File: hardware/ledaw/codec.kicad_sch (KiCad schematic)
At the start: 50 parts, among them U1 MAX98089ETN_T, Y1 SG-210SCD

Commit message: hw: headphone and wip mic
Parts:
- removed TP1: JACKSENSE, symbol Connector:TestPoint_2Pole
- removed TP11: FSPKRN, symbol Connector:TestPoint_2Pole
- removed TP2: RXP, symbol Connector:TestPoint_2Pole
- removed TP3: RXN, symbol Connector:TestPoint_2Pole
- removed TP5: FSPKLP, symbol Connector:TestPoint_2Pole
- removed TP7: FSPKLN, symbol Connector:TestPoint_2Pole
- removed TP9: FSPKRP, symbol Connector:TestPoint_2Pole
- added C16, C17: 10pF, symbol Device:C_Small
- added C18: 2.2uF, symbol Device:C_Small
- added C19, C20, C21, C22: 1uF, symbol Device:C_Small
- added J1: HEADPHONE, symbol Connector_Audio:AudioJack3_Ground
- added JP1, JP2, JP3: (no value), symbol Jumper:Jumper_2_Small_Open
- added R11, R12, R13, R14: 0, symbol Device:R_Small
- added R15: OPEN, symbol Device:R_Small
- added R16: 10k, symbol Device:R_Small
- added R17, R18: 2.2k, symbol Device:R_Small
- added TP1: JACKSENSE, symbol Connector:TestPoint
- added TP11: FSPKRN, symbol Connector:TestPoint
- added TP12: HPR, symbol Connector:TestPoint
- added TP13: HPL, symbol Connector:TestPoint
- added TP14: HPGND, symbol Connector:TestPoint
- added TP2: RXP, symbol Connector:TestPoint
- added TP3: RXN, symbol Connector:TestPoint
- added TP5: FSPKLP, symbol Connector:TestPoint
- added TP7: FSPKLN, symbol Connector:TestPoint
- added TP9: FSPKRP, symbol Connector:TestPoint
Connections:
- net GND: now also R5.2, U1.16 (SPKRGND), U1.21 (SPKLGND), U1.3 (DGND), U1.30 (HPGND), U1.47 (AGND), U1.57 (EP), C16.2, C17.2, C18.2, C19.2, C21.1, C22.1
- net JACKSNS: now also JP3.1 (A), TP1.1
- net at C5.1, C7.2, L2.2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: now also TP7.1
- net at C15.1, C9.1, L3.2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: now also TP9.1
- net at C1.1, L1.1, TP4.1: now also R7.1; no longer R3.1
- net at C2.1, C7.1, L1.2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: now also TP5.1
- net at R2.1: now also TP3.1
- net at C8.1, L3.1, TP8.1: now also R11.1; no longer R7.1
- net at R7.2: now also U1.20 (SPKLP); no longer U1.17 (SPKRP)
- net at C4.1, L2.1, TP6.1: now also R9.1; no longer R5.1
- net at C11.1, L4.1, TP10.1: now also R12.1; no longer R9.1
- net at C13.1, C15.2, L4.2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: now also TP11.1
- net at R9.2: now also U1.22 (SPKLN); no longer U1.15 (SPKRN)
- net HPGND: now reaches R3.2
- net HPGND: now also R5.1, J1.G, TP14.1; no longer U1.20 (SPKLP)
- net C1P: now reaches U1.26 (C1P)
- net C1P: now also C20.2
- net C1N: now reaches U1.27 (C1N)
- net C1N: now also C20.1
- net HPVSS: now reaches U1.31 (HPVSS)
- net HPVSS: now also C21.2
- net HPVDD: now reaches U1.32 (HPVDD)
- net at U1.33 (HPL): now also C17.1, R14.2
- net at U1.34 (HPSNS): now also R3.1
- net at U1.35 (HPR): now also C16.1, R13.2
- net at U1.44 (MICBIAS): now also C22.2, JP2.2 (B), R18.1
- net at U1.48 (REF): now also C18.1
- net at U1.49 (REG): now also C19.1
- net CODEC_~{IRQ}: now reaches U1.56 (~{IRQ})
- net CODEC_~{IRQ}: now also R15.1, R16.1
- net at R1.1: now also TP2.1
- new net: J1.R, R13.1, TP12.1
- new net: J1.S, JP1.2 (B)
- new net: R12.2, U1.15 (SPKRN)
- new net: JP3.2 (B), R17.2
- new net: J1.T, R14.1, TP13.1
- new net: JP2.1 (A), R17.1
- new net: R11.2, U1.17 (SPKRP)
- new net +1V8: R15.2
- new net +3V3: R16.2
- new net MIC1P: JP1.1 (A)
- new net MIC2P: R18.2
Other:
- note added: "TODO conn HPND pin to net?"
- moved on the sheet: TP4

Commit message: hw: big simplification
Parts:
- removed C100: 10uF, symbol Device:C_Small
- removed C16, C17: 10pF, symbol Device:C_Small
- removed C22: 1uF, symbol Device:C_Small
- removed J1: HEADPHONE, symbol Connector_Audio:AudioJack3_Ground
- removed JP1, JP2, JP3: (no value), symbol Jumper:Jumper_2_Small_Open
- removed R13, R14, R3, R5: 0, symbol Device:R_Small
- removed R15: OPEN, symbol Device:R_Small
- removed R18: 2.2k, symbol Device:R_Small
- added C108, C109: 1uF, symbol Device:C_Small
- added C23: 10uF, symbol Device:C_Small
- added J2: AudioJack4, symbol Connector_Audio:AudioJack4
- added TP15: MIC2P, symbol Connector:TestPoint
- added TP16: MIC2N, symbol Connector:TestPoint
- added TP17: MICBIAS, symbol Connector:TestPoint
- added TP18: HPSNS, symbol Connector:TestPoint
- C102, C106: value 1uF -> 0.1uF
- C12: value 0.1uF -> 1uF
- TP2: value RXP -> RECP
- TP3: value RXN -> RECN
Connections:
- net AVDD is gone; now on net +1V8: C103.2, U1.50 (AVDD)
- net DVDD is gone; now on net +1V8: C101.2, U1.53 (DVDD)
- net DVDDS1 is gone; now on net +3V3: C102.2, U1.6 (DVDDS1)
- net DVDDS2 is gone; now on net +3V3: C106.2, U1.55 (DVDDS2)
- net JACKSNS is gone; now on net JackS: TP1.1, U1.45 (JACKSNS)
- net PVDD is gone; now on net +1V8: C12.2, U1.25 (PVDD)
- net +1V8: now also C23.2
- net GND: now also U1.34 (HPSNS), C109.1, C23.1, J2.R2, TP16.1, TP18.1
- net at TP12.1: now also U1.35 (HPR), J2.R1
- net at U1.33 (HPL): now also TP13.1, J2.T
- net at U1.44 (MICBIAS): now also R17.1
- net JackS: now reaches R17.2
- net JackS: now also C108.1, J2.S, TP15.1, TP17.1
- net at U1.42 (MIC2P): now also C108.2
- net at U1.43 (MIC2N): now also C109.2
- net SPKVDD renamed +5V
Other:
- moved on the sheet: C107, R16, TP12, TP13, Y1

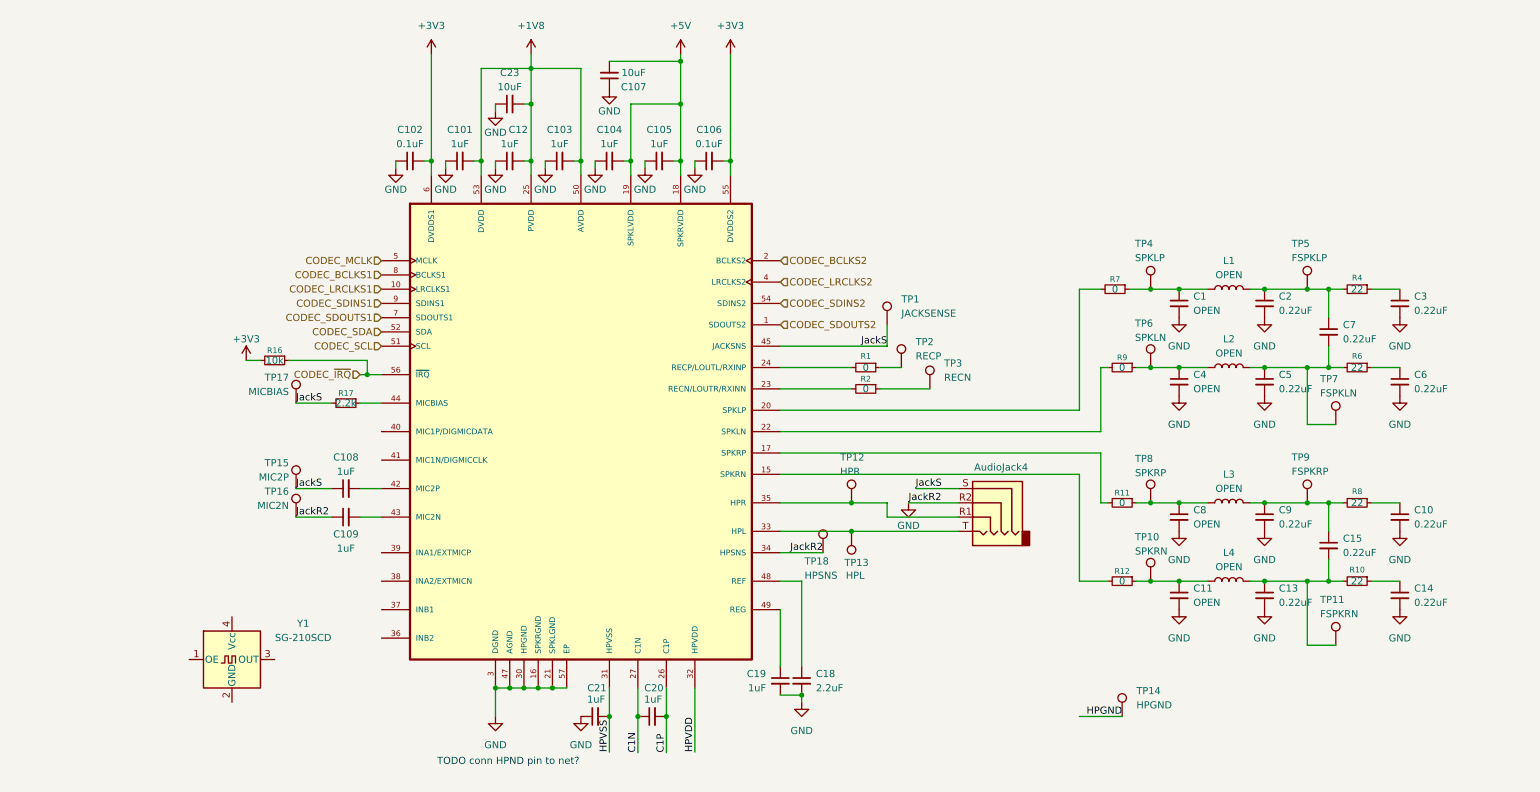
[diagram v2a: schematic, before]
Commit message: hw: speakers, line in/out. only missing digital mic now
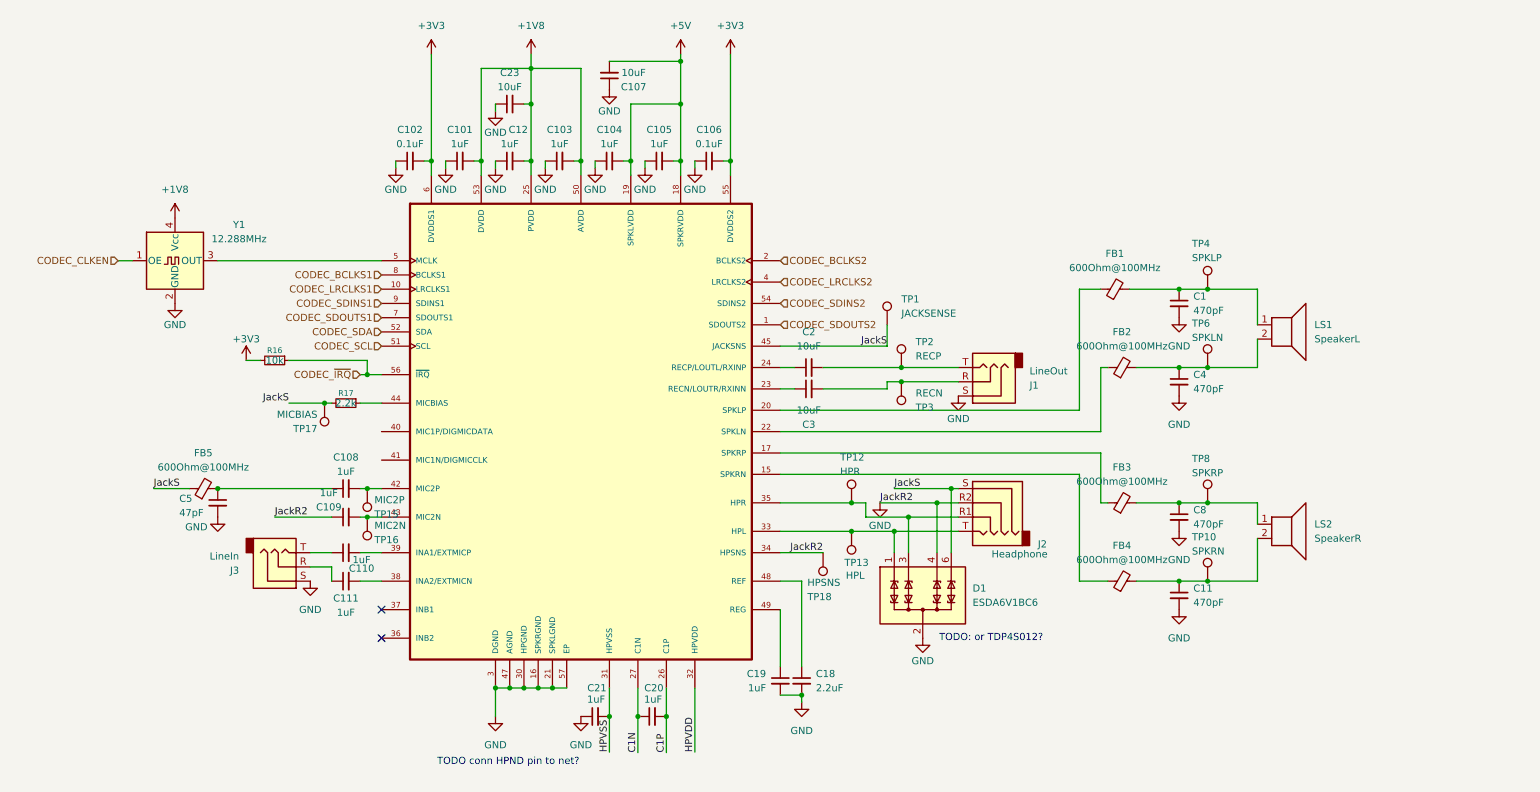
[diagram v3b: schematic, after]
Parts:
- removed C10, C13, C14, C15, C6, C7, C9: 0.22uF, symbol Device:C_Small
- removed L1, L2, L3, L4: OPEN, symbol Device:L
- removed R1, R11, R12, R2, R7, R9: 0, symbol Device:R_Small
- removed R10, R4, R6, R8: 22, symbol Device:R_Small
- removed TP11: FSPKRN, symbol Connector:TestPoint
- removed TP14: HPGND, symbol Connector:TestPoint
- removed TP5: FSPKLP, symbol Connector:TestPoint
- removed TP7: FSPKLN, symbol Connector:TestPoint
- removed TP9: FSPKRP, symbol Connector:TestPoint
- added C110, C111: 1uF, symbol Device:C_Small
- added D1: ESDA6V1BC6, Package_TO_SOT_SMD:SOT-23-6, symbol Power_Protection:ESDA6V1BC6
- added FB1, FB2, FB3, FB4, FB5: 600Ohm@100MHz, symbol Device:FerriteBead_Small
- added J1: LineOut, symbol Connector_Audio:AudioJack3
- added J3: LineIn, symbol Connector_Audio:AudioJack3
- added LS1: SpeakerL, symbol Device:Speaker
- added LS2: SpeakerR, symbol Device:Speaker
- C1, C11, C4, C8: value OPEN -> 470pF
- C2, C3: value 0.22uF -> 10uF
- C5: value 0.22uF -> 47pF
- J2: value AudioJack4 -> Headphone
- Y1: value SG-210SCD -> 12.288MHz
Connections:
- net CODEC_MCLK is gone; now on an unnamed net: U1.5 (MCLK)
- net +1V8: now also Y1.4 (Vcc)
- net GND: now also Y1.2 (GND), D1.2 (COM), D1.4 (TVS3), D1.5 (COM), J1.S, J3.S; no longer C2.2, C3.2, TP16.1
- net JackS: now also D1.6 (TVS4), FB5.1; no longer C108.1, TP15.1
- net at J2.R1, TP12.1, U1.35 (HPR): now also D1.3 (TVS2)
- net at C5.1: now also C108.1, FB5.2
- net at J2.T, TP13.1, U1.33 (HPL): now also D1.1 (TVS1)
- net at C1.1, TP4.1: now also FB1.2, LS1.1
- net at C2.1: now also U1.24 (RECP/LOUTL/RXINP)
- net at C4.1, TP6.1: now also FB2.2, LS1.2
- net at U1.22 (SPKLN): now also FB2.1
- net at TP3.1: now also C3.2, J1.R
- net at U1.23 (RECN/LOUTR/RXINN): now also C3.1
- net at C8.1, TP8.1: now also FB3.2, LS2.1
- net at C11.1, TP10.1: now also FB4.2, LS2.2
- net at U1.15 (SPKRN): now also FB4.1
- net at TP2.1: now also C2.2, J1.T
- net at U1.20 (SPKLP): now also FB1.1
- net CODEC_CLKEN: now reaches Y1.1 (OE)
- net at U1.17 (SPKRP): now also FB3.1
- net at U1.38 (INA2/EXTMICN): now also C111.2
- net at U1.39 (INA1/EXTMICP): now also C110.2
- net at C108.2, U1.42 (MIC2P): now also TP15.1
- net at C109.2, U1.43 (MIC2N): now also TP16.1
- new net: C110.1, J3.T
- new net: C111.1, J3.R
- no-connect marks 0 -> 2
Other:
- note added: "TODO: or TDP4S012?"
- moved on the sheet: TP10, TP18, TP4, TP6, TP8, Y1

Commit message: hw: done codec?
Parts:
- added C22: 1uF, symbol Device:C_Small
- added C6, C7: 0.1uF X7R, symbol Device:C_Small
- added MK1: MicL, Sensor_Audio:Knowles_LGA-5_3.5x2.65mm, symbol Sensor_Audio:SPH0641LU4H-1
- added MK2: MicR, Sensor_Audio:Knowles_LGA-5_3.5x2.65mm, symbol Sensor_Audio:SPH0641LU4H-1
- added TP19: CODEC_MCLK, symbol Connector:TestPoint
- added TP20: INA1, symbol Connector:TestPoint
- added TP21: INA2, symbol Connector:TestPoint
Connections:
- net CODEC_SDINS2 is gone; now on net GND: U1.54 (SDINS2)
- net +1V8: now also C6.2, C7.2, MK1.5 (VDD), MK2.2 (SEL), MK2.5 (VDD)
- net GND: now also C21.2, C22.2, C6.1, C7.1, MK1.2 (SEL), MK1.3 (GND), MK2.3 (GND); no longer C21.1
- net at C110.2, U1.39 (INA1/EXTMICP): now also TP20.1
- net at U1.5 (MCLK), Y1.3 (OUT): now also TP19.1
- net at C111.2, U1.38 (INA2/EXTMICN): now also TP21.1
- net DIGMICDATA: now reaches U1.40 (MIC1P/DIGMICDATA)
- net DIGMICDATA: now also MK1.1 (DATA), MK2.1 (DATA)
- net DIGMICCLK: now reaches U1.41 (MIC1N/DIGMICCLK)
- net DIGMICCLK: now also MK1.4 (CLOCK), MK2.4 (CLOCK)
- net CODEC_BCLKS2: no longer names the net of U1.2 (BCLKS2)
- net CODEC_LRCLKS2: no longer names the net of U1.4 (LRCLKS2)
- net CODEC_SDOUTS2: no longer names the net of U1.1 (SDOUTS2)
- net HPVDD: no longer names the net of U1.32 (HPVDD)
- net HPVDD: now also C22.1
- net HPVSS: no longer names the net of U1.31 (HPVSS)
- net HPVSS: now also C21.1; no longer C21.2
- no-connect marks 2 -> 5
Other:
- note removed: "TODO conn HPND pin to net?"
- moved on the sheet: C1, C101, C102, C103, C104, C105, C106, C107, C108, C109, C11, C110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
